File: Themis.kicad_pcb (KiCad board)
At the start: 2 copper layers, 100 x 50 mm, 568 parts, among them J1 SMA, J10 Conn_01x01, J11 Conn_01x01, J12 Conn_01x01, J13 Conn_01x01, J14 SMA, J15 SMA, J16 SMA, J17 SMA, J18 Conn_01x01, J2 SMA, J20 Conn_01x01, J3 SMA, J4 SMA, J5 Conn_01x05, J6 SMA, J7 SMA, J8 SMA, J9 SMA, T1 Tr 1/33, T2 Tr 33/1, U1 LMC6482

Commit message: preparing themis v2
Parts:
- removed C6: 10n, Capacitors_SMD:C_0805_HandSoldering
- removed J1, J14, J3, J6: SMA, SMA_PINS:SMA_EDGE_NRW
- removed J15, J16, J2, J4, J9: SMA, SMA_PINS:SMA_PINS
- removed L1: L_Small, Inductors_SMD:L_0805_HandSoldering
- removed the REF** at (186.0, 94.0)
- removed the REF** at (187.0, 98.0)
- removed the REF** at (120.0, 90.0)
- removed the REF** at (119.0, 90.0)
- removed the REF** at (118.0, 90.0)
- removed the REF** at (117.0, 90.0)
- removed the REF** at (116.0, 90.0)
- removed the REF** at (115.0, 90.0)
- removed the REF** at (114.0, 90.0)
- removed the REF** at (113.0, 90.0)
- removed the REF** at (112.0, 90.0)
- removed the REF** at (111.0, 90.0)
- removed the REF** at (186.0, 99.0)
- removed the REF** at (110.0, 90.0)
- removed the REF** at (109.0, 90.0)
- removed the REF** at (108.0, 90.0)
- removed the REF** at (107.0, 90.0)
- removed the REF** at (106.0, 90.0)
- removed the REF** at (105.0, 90.0)
- removed the REF** at (104.0, 90.0)
- removed the REF** at (103.0, 90.0)
- removed the REF** at (102.0, 90.0)
- removed the REF** at (101.0, 90.0)
- removed the REF** at (187.0, 99.0)
- removed the REF** at (100.0, 90.0)
- removed the REF** at (99.0, 90.0)
- removed the REF** at (127.0, 89.0)
- removed the REF** at (126.0, 89.0)
- removed the REF** at (125.0, 89.0)
- removed the REF** at (124.0, 89.0)
- removed the REF** at (123.0, 89.0)
- removed the REF** at (122.0, 89.0)
- removed the REF** at (121.0, 89.0)
- removed the REF** at (120.0, 89.0)
- removed the REF** at (186.0, 100.0)
- removed the REF** at (119.0, 89.0)
- removed the REF** at (118.0, 89.0)
- removed the REF** at (117.0, 89.0)
- removed the REF** at (116.0, 89.0)
- removed the REF** at (115.0, 89.0)
- removed the REF** at (114.0, 89.0)
- removed the REF** at (113.0, 89.0)
- removed the REF** at (112.0, 89.0)
- removed the REF** at (111.0, 89.0)
- removed the REF** at (110.0, 89.0)
- removed the REF** at (187.0, 100.0)
- removed the REF** at (109.0, 89.0)
- removed the REF** at (108.0, 89.0)
- removed the REF** at (107.0, 89.0)
- removed the REF** at (106.0, 89.0)
- removed the REF** at (105.0, 89.0)
- removed the REF** at (104.0, 89.0)
- removed the REF** at (103.0, 89.0)
- removed the REF** at (102.0, 89.0)
- removed the REF** at (101.0, 89.0)
- removed the REF** at (100.0, 89.0)
- removed the REF** at (188.0, 94.0)
- removed the REF** at (99.0, 89.0)
- removed the REF** at (127.0, 88.0)
- removed the REF** at (126.0, 88.0)
- removed the REF** at (125.0, 88.0)
- removed the REF** at (124.0, 88.0)
- removed the REF** at (123.0, 88.0)
- removed the REF** at (122.0, 88.0)
- removed the REF** at (121.0, 88.0)
- removed the REF** at (120.0, 88.0)
- removed the REF** at (119.0, 88.0)
- removed the REF** at (188.0, 95.0)
- removed the REF** at (118.0, 88.0)
- removed the REF** at (117.0, 88.0)
- removed the REF** at (116.0, 88.0)
- removed the REF** at (115.0, 88.0)
- removed the REF** at (114.0, 88.0)
- removed the REF** at (113.0, 88.0)
- removed the REF** at (112.0, 88.0)
- removed the REF** at (111.0, 88.0)
- removed the REF** at (110.0, 88.0)
- removed the REF** at (109.0, 88.0)
- removed the REF** at (188.0, 96.0)
- removed the REF** at (108.0, 88.0)
- removed the REF** at (107.0, 88.0)
- removed the REF** at (106.0, 88.0)
- removed the REF** at (105.0, 88.0)
- removed the REF** at (104.0, 88.0)
- removed the REF** at (103.0, 88.0)
- removed the REF** at (102.0, 88.0)
- removed the REF** at (101.0, 88.0)
- removed the REF** at (100.0, 88.0)
- removed the REF** at (99.0, 88.0)
- removed the REF** at (188.0, 97.0)
- removed the REF** at (127.0, 87.0)
- removed the REF** at (126.0, 87.0)
- removed the REF** at (125.0, 87.0)
- removed the REF** at (124.0, 87.0)
- removed the REF** at (123.0, 87.0)
- removed the REF** at (122.0, 87.0)
- removed the REF** at (121.0, 87.0)
- removed the REF** at (120.0, 87.0)
- removed the REF** at (119.0, 87.0)
- removed the REF** at (118.0, 87.0)
- removed the REF** at (188.0, 98.0)
- removed the REF** at (117.0, 87.0)
- removed the REF** at (116.0, 87.0)
- removed the REF** at (115.0, 87.0)
- removed the REF** at (114.0, 87.0)
- removed the REF** at (113.0, 87.0)
- removed the REF** at (112.0, 87.0)
- removed the REF** at (111.0, 87.0)
- removed the REF** at (110.0, 87.0)
- removed the REF** at (109.0, 87.0)
- removed the REF** at (108.0, 87.0)
- removed the REF** at (187.0, 94.0)
- removed the REF** at (188.0, 99.0)
- removed the REF** at (107.0, 87.0)
- removed the REF** at (106.0, 87.0)
- removed the REF** at (105.0, 87.0)
- removed the REF** at (104.0, 87.0)
- removed the REF** at (103.0, 87.0)
- removed the REF** at (102.0, 87.0)
- removed the REF** at (101.0, 87.0)
- removed the REF** at (100.0, 87.0)
- removed the REF** at (99.0, 87.0)
- removed the REF** at (91.0, 101.0)
- removed the REF** at (188.0, 100.0)
- removed the REF** at (91.0, 100.0)
- removed the REF** at (91.0, 99.0)
- removed the REF** at (91.0, 98.0)
- removed the REF** at (91.0, 97.0)
- removed the REF** at (91.0, 96.0)
- removed the REF** at (91.0, 95.0)
- removed the REF** at (91.0, 94.0)
- removed the REF** at (91.0, 93.0)
- removed the REF** at (91.0, 92.0)
- removed the REF** at (91.0, 91.0)
- removed the REF** at (93.0, 94.0)
- removed the REF** at (91.0, 90.0)
- removed the REF** at (91.0, 89.0)
- removed the REF** at (91.0, 88.0)
- removed the REF** at (91.0, 87.0)
- removed the REF** at (189.0, 101.0)
- removed the REF** at (189.0, 100.0)
- removed the REF** at (189.0, 99.0)
- removed the REF** at (189.0, 98.0)
- removed the REF** at (189.0, 97.0)
- removed the REF** at (189.0, 96.0)
- removed the REF** at (94.0, 94.0)
- removed the REF** at (189.0, 95.0)
- removed the REF** at (189.0, 94.0)
- removed the REF** at (189.0, 93.0)
- removed the REF** at (189.0, 92.0)
- removed the REF** at (189.0, 91.0)
- removed the REF** at (189.0, 90.0)
- removed the REF** at (189.0, 89.0)
- removed the REF** at (189.0, 88.0)
- removed the REF** at (189.0, 87.0)
- removed the REF** at (189.0, 133.0)
- removed the REF** at (95.0, 94.0)
- removed the REF** at (189.0, 132.0)
- removed the REF** at (189.0, 131.0)
- removed the REF** at (189.0, 130.0)
- removed the REF** at (189.0, 129.0)
- removed the REF** at (189.0, 128.0)
- removed the REF** at (189.0, 127.0)
- removed the REF** at (189.0, 126.0)
- removed the REF** at (189.0, 125.0)
- removed the REF** at (189.0, 124.0)
- removed the REF** at (189.0, 123.0)
- removed the REF** at (93.0, 95.0)
- removed the REF** at (189.0, 122.0)
- removed the REF** at (189.0, 121.0)
- removed the REF** at (189.0, 120.0)
- removed the REF** at (189.0, 119.0)
- removed the REF** at (189.0, 118.0)
- removed the REF** at (189.0, 117.0)
- removed the REF** at (189.0, 116.0)
- removed the REF** at (189.0, 115.0)
- removed the REF** at (189.0, 114.0)
- removed the REF** at (189.0, 113.0)
- removed the REF** at (94.0, 95.0)
- removed the REF** at (189.0, 112.0)
- removed the REF** at (189.0, 111.0)
- removed the REF** at (189.0, 110.0)
- removed the REF** at (188.5, 134.0)
- removed the REF** at (187.5, 134.0)
- removed the REF** at (186.5, 134.0)
- removed the REF** at (185.5, 134.0)
- removed the REF** at (184.5, 134.0)
- removed the REF** at (183.5, 134.0)
- removed the REF** at (182.5, 134.0)
- removed the REF** at (95.0, 95.0)
- removed the REF** at (181.5, 134.0)
- removed the REF** at (180.5, 134.0)
- removed the REF** at (179.5, 134.0)
- removed the REF** at (178.5, 134.0)
- removed the REF** at (177.5, 134.0)
- removed the REF** at (176.5, 134.0)
- removed the REF** at (168.5, 134.0)
- removed the REF** at (167.5, 134.0)
- removed the REF** at (166.5, 134.0)
- removed the REF** at (165.5, 134.0)
- removed the REF** at (93.0, 96.0)
- removed the REF** at (164.5, 134.0)
- removed the REF** at (163.5, 134.0)
- removed the REF** at (162.5, 134.0)
- removed the REF** at (161.5, 134.0)
- removed the REF** at (160.5, 134.0)
- removed the REF** at (159.5, 134.0)
- removed the REF** at (158.5, 134.0)
- removed the REF** at (157.5, 134.0)
- removed the REF** at (156.5, 134.0)
- removed the REF** at (155.5, 134.0)
- removed the REF** at (94.0, 96.0)
- removed the REF** at (154.5, 134.0)
- removed the REF** at (153.5, 134.0)
- removed the REF** at (152.5, 134.0)
- removed the REF** at (151.5, 134.0)
- removed the REF** at (150.5, 134.0)
- removed the REF** at (149.5, 134.0)
- removed the REF** at (148.5, 134.0)
- removed the REF** at (147.5, 134.0)
- removed the REF** at (146.5, 134.0)
- removed the REF** at (145.5, 134.0)
- removed the REF** at (186.0, 95.0)
- removed the REF** at (95.0, 96.0)
- removed the REF** at (144.5, 134.0)
- removed the REF** at (143.5, 134.0)
- removed the REF** at (142.5, 134.0)
- removed the REF** at (141.5, 134.0)
- removed the REF** at (104.5, 134.0)
- removed the REF** at (103.5, 134.0)
- removed the REF** at (102.5, 134.0)
- removed the REF** at (101.5, 134.0)
- removed the REF** at (100.5, 134.0)
- removed the REF** at (99.5, 134.0)
- removed the REF** at (93.0, 97.0)
- removed the REF** at (98.5, 134.0)
- removed the REF** at (97.5, 134.0)
- removed the REF** at (96.5, 134.0)
- removed the REF** at (95.5, 134.0)
- removed the REF** at (94.5, 134.0)
- removed the REF** at (93.5, 134.0)
- removed the REF** at (92.5, 134.0)
- removed the REF** at (91.5, 134.0)
- removed the REF** at (91.5, 133.0)
- removed the REF** at (91.5, 132.0)
- removed the REF** at (94.0, 97.0)
- removed the REF** at (91.5, 131.0)
- removed the REF** at (91.5, 130.0)
- removed the REF** at (91.5, 129.0)
- removed the REF** at (91.5, 128.0)
- removed the REF** at (91.5, 127.0)
- removed the REF** at (91.5, 126.0)
- removed the REF** at (91.5, 125.0)
- removed the REF** at (91.5, 124.0)
- removed the REF** at (91.5, 123.0)
- removed the REF** at (91.5, 122.0)
- removed the REF** at (95.0, 97.0)
- removed the REF** at (91.5, 121.0)
- removed the REF** at (91.5, 120.0)
- removed the REF** at (91.5, 119.0)
- removed the REF** at (91.5, 118.0)
- removed the REF** at (91.5, 117.0)
- removed the REF** at (91.5, 116.0)
- removed the REF** at (91.5, 115.0)
- removed the REF** at (91.5, 114.0)
- removed the REF** at (91.5, 113.0)
- removed the REF** at (91.5, 112.0)
- removed the REF** at (93.0, 98.0)
- removed the REF** at (91.5, 111.0)
- removed the REF** at (91.5, 110.0)
- removed the REF** at (91.5, 109.0)
- removed the REF** at (189.0, 86.0)
- removed the REF** at (188.0, 86.0)
- removed the REF** at (187.0, 86.0)
- removed the REF** at (186.0, 86.0)
- removed the REF** at (185.0, 86.0)
- removed the REF** at (184.0, 86.0)
- removed the REF** at (183.0, 86.0)
- removed the REF** at (94.0, 98.0)
- removed the REF** at (182.0, 86.0)
- removed the REF** at (181.0, 86.0)
- removed the REF** at (180.0, 86.0)
- removed the REF** at (179.0, 86.0)
- removed the REF** at (178.0, 86.0)
- removed the REF** at (177.0, 86.0)
- removed the REF** at (176.0, 86.0)
- removed the REF** at (175.0, 86.0)
- removed the REF** at (174.0, 86.0)
- removed the REF** at (173.0, 86.0)
- removed the REF** at (95.0, 98.0)
- removed the REF** at (172.0, 86.0)
- removed the REF** at (171.0, 86.0)
- removed the REF** at (170.0, 86.0)
- removed the REF** at (169.0, 86.0)
- removed the REF** at (168.0, 86.0)
- removed the REF** at (167.0, 86.0)
- removed the REF** at (166.0, 86.0)
- removed the REF** at (165.0, 86.0)
- removed the REF** at (164.0, 86.0)
- removed the REF** at (163.0, 86.0)
- removed the REF** at (93.0, 99.0)
- removed the REF** at (162.0, 86.0)
- removed the REF** at (161.0, 86.0)
- removed the REF** at (160.0, 86.0)
- removed the REF** at (159.0, 86.0)
- removed the REF** at (158.0, 86.0)
- removed the REF** at (157.0, 86.0)
- removed the REF** at (156.0, 86.0)
- removed the REF** at (155.0, 86.0)
- removed the REF** at (154.0, 86.0)
- removed the REF** at (153.0, 86.0)
- removed the REF** at (94.0, 99.0)
- removed the REF** at (152.0, 86.0)
- removed the REF** at (151.0, 86.0)
- removed the REF** at (150.0, 86.0)
- removed the REF** at (149.0, 86.0)
- removed the REF** at (148.0, 86.0)
- removed the REF** at (147.0, 86.0)
- removed the REF** at (146.0, 86.0)
- removed the REF** at (145.0, 86.0)
- removed the REF** at (144.0, 86.0)
- removed the REF** at (143.0, 86.0)
- removed the REF** at (95.0, 99.0)
- removed the REF** at (142.0, 86.0)
- removed the REF** at (141.0, 86.0)
- removed the REF** at (140.0, 86.0)
- removed the REF** at (139.0, 86.0)
- removed the REF** at (138.0, 86.0)
- removed the REF** at (137.0, 86.0)
- removed the REF** at (136.0, 86.0)
- removed the REF** at (135.0, 86.0)
- removed the REF** at (134.0, 86.0)
- removed the REF** at (133.0, 86.0)
- removed the REF** at (187.0, 95.0)
- removed the REF** at (92.0, 94.0)
- removed the REF** at (132.0, 86.0)
- removed the REF** at (131.0, 86.0)
- removed the REF** at (130.0, 86.0)
- removed the REF** at (129.0, 86.0)
- removed the REF** at (128.0, 86.0)
- removed the REF** at (127.0, 86.0)
- removed the REF** at (126.0, 86.0)
- removed the REF** at (125.0, 86.0)
- removed the REF** at (124.0, 86.0)
- removed the REF** at (123.0, 86.0)
- removed the REF** at (92.0, 95.0)
- removed the REF** at (122.0, 86.0)
- removed the REF** at (121.0, 86.0)
- removed the REF** at (120.0, 86.0)
- removed the REF** at (119.0, 86.0)
- removed the REF** at (118.0, 86.0)
- removed the REF** at (117.0, 86.0)
- removed the REF** at (116.0, 86.0)
- removed the REF** at (115.0, 86.0)
- removed the REF** at (114.0, 86.0)
- removed the REF** at (113.0, 86.0)
- removed the REF** at (92.0, 96.0)
- removed the REF** at (112.0, 86.0)
- removed the REF** at (111.0, 86.0)
- removed the REF** at (110.0, 86.0)
- removed the REF** at (109.0, 86.0)
- removed the REF** at (108.0, 86.0)
- removed the REF** at (107.0, 86.0)
- removed the REF** at (106.0, 86.0)
- removed the REF** at (105.0, 86.0)
- removed the REF** at (104.0, 86.0)
- removed the REF** at (103.0, 86.0)
- removed the REF** at (92.0, 97.0)
- removed the REF** at (102.0, 86.0)
- removed the REF** at (101.0, 86.0)
- removed the REF** at (100.0, 86.0)
- removed the REF** at (99.0, 86.0)
- removed the REF** at (98.0, 86.0)
- removed the REF** at (97.0, 86.0)
- removed the REF** at (96.0, 86.0)
- removed the REF** at (95.0, 86.0)
- removed the REF** at (94.0, 86.0)
- removed the REF** at (93.0, 86.0)
- removed the REF** at (92.0, 98.0)
- removed the REF** at (92.0, 86.0)
- removed the REF** at (94.5, 126.0)
- removed the REF** at (93.5, 126.0)
- removed the REF** at (92.5, 126.0)
- removed the REF** at (94.5, 125.0)
- removed the REF** at (93.5, 125.0)
- removed the REF** at (92.5, 125.0)
- removed the REF** at (94.5, 124.0)
- removed the REF** at (93.5, 124.0)
- removed the REF** at (92.5, 124.0)
- removed the REF** at (92.0, 99.0)
- removed the REF** at (94.5, 123.0)
- removed the REF** at (93.5, 123.0)
- removed the REF** at (92.5, 123.0)
- removed the REF** at (94.5, 122.0)
- removed the REF** at (93.5, 122.0)
- removed the REF** at (92.5, 122.0)
- removed the REF** at (94.5, 121.0)
- removed the REF** at (93.5, 121.0)
- removed the REF** at (92.5, 121.0)
- removed the REF** at (94.5, 120.0)
- removed the REF** at (188.0, 128.0)
- removed the REF** at (93.5, 120.0)
- removed the REF** at (92.5, 120.0)
- removed the REF** at (94.5, 119.0)
- removed the REF** at (93.5, 119.0)
- removed the REF** at (92.5, 119.0)
- removed the REF** at (94.5, 118.0)
- removed the REF** at (93.5, 118.0)
- removed the REF** at (92.5, 118.0)
- removed the REF** at (94.5, 117.0)
- removed the REF** at (93.5, 117.0)
- removed the REF** at (188.0, 127.0)
- removed the REF** at (92.5, 117.0)
- removed the REF** at (94.5, 116.0)
- removed the REF** at (93.5, 116.0)
- removed the REF** at (92.5, 116.0)
- removed the REF** at (94.5, 115.0)
- removed the REF** at (93.5, 115.0)
- removed the REF** at (92.5, 115.0)
- removed the REF** at (94.5, 114.0)
- removed the REF** at (93.5, 114.0)
- removed the REF** at (92.5, 114.0)
- removed the REF** at (188.0, 126.0)
- removed the REF** at (94.5, 113.0)
- removed the REF** at (93.5, 113.0)
- removed the REF** at (92.5, 113.0)
- removed the REF** at (94.5, 112.0)
- removed the REF** at (93.5, 112.0)
- removed the REF** at (92.5, 112.0)
- removed the REF** at (94.5, 111.0)
- removed the REF** at (93.5, 111.0)
- removed the REF** at (187.0, 126.0)
- removed the REF** at (186.0, 126.0)
- removed the REF** at (188.0, 125.0)
- removed the REF** at (187.0, 125.0)
- removed the REF** at (186.0, 125.0)
- removed the REF** at (187.0, 124.0)
- removed the REF** at (186.0, 124.0)
- removed the REF** at (187.0, 123.0)
- removed the REF** at (186.0, 123.0)
- removed the REF** at (187.0, 122.0)
- removed the REF** at (186.0, 122.0)
- removed the REF** at (187.0, 121.0)
- removed the REF** at (186.0, 121.0)
- removed the REF** at (186.0, 96.0)
- removed the REF** at (188.0, 124.0)
- removed the REF** at (187.0, 120.0)
- removed the REF** at (186.0, 120.0)
- removed the REF** at (187.0, 119.0)
- removed the REF** at (186.0, 119.0)
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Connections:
- J5 pad 5: TX_RX_RLY -> (no net)
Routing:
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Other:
- board text added: "Themis Θέμις V2.0"
- board text removed: "HPF out"
- board text removed: "PS_IN"
- board text removed: "RX1_Line"
- board text removed: "Themis Θέμις"

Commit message: Themis V2
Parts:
- removed REF**: via, via:via
- C2, C3, C4, C5, D1, D2, D3, D4, R10, R11, R12, R13, R4, R5, R6, R7, R8, R9: moved to B.Cu
- J17, J8: footprint SMA_PINS:SMA_EDGE_NRW -> SMA_PINS:SMA_PINS
- U1: footprint Housings_SOIC:SOIC-8_3.9x4.9mm_Pitch1.27mm -> Package_SO:SOIC-8_3.9x4.9mm_P1.27mm; moved to B.Cu
- moved R6 19.7 mm to (149.5, 127.0), turned to 180 degrees
- moved J5 17.0 mm to (143.0, 130.5)
- moved C3 12.3 mm to (160.5, 123.0), turned to 270 degrees
- moved R11 12.0 mm to (158.5, 118.0), turned to 90 degrees
- moved D2 11.8 mm to (155.0, 126.0), turned to 270 degrees
- moved C2 10.1 mm to (155.2, 131.5), turned to 90 degrees
- moved T1 10.0 mm to (170.0, 105.0)
- moved R7 9.71 mm to (163.0, 123.0), turned to 270 degrees
- moved R5 9.49 mm to (159.5, 131.5), turned to 270 degrees
- moved U1 8.85 mm to (150.0, 121.5), turned to 90 degrees
- moved R12 8.50 mm to (142.0, 122.5), turned to 90 degrees
- moved R9 8.06 mm to (130.5, 118.5), turned to 180 degrees
- moved D1 8.00 mm to (161.5, 118.0), turned to 180 degrees
- moved R10 7.50 mm to (134.0, 115.0)
- moved R8 7.50 mm to (138.5, 114.5)
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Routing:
- net GND: track 375.5 -> 308.9 mm, vias 312 -> 258
- net (no net): track 27.1 -> 3.05 mm, vias 21 -> 0
- net Net-(J8-Pad1): track 23.5 -> 8.51 mm
- net Net-(C2-Pad2): track 10.1 -> 23.7 mm
- net Net-(C3-Pad1): track 9.81 -> 19.8 mm
- net Net-(D1-Pad2): track 37.9 -> 29.7 mm
- net +12V: track 18.8 -> 26.3 mm
- net Net-(C1-Pad2): track 74.0 -> 81.2 mm
- net Net-(D4-Pad2): track 7.96 -> 14.8 mm
- net Net-(D2-Pad2): track 8.36 -> 11.4 mm
- net Net-(C4-Pad1): track 16.8 -> 13.8 mm
- net Net-(D3-Pad2): track 9.31 -> 6.82 mm
- net Net-(C5-Pad2): track 12.9 -> 11.3 mm
- net Net-(D4-Pad1): track 10.1 -> 11.5 mm
- net Net-(D2-Pad1): track 11.8 -> 10.5 mm
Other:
- board text added: "In"
- board text added: "LPF_ Out"
- board text added: "Out"
- board text added: "PS_ Feedback"
- board text added: "TX_ Coax_ Out"
- board text removed: "LPF_Out"
- board text removed: "PS_Feedback"
- board text removed: "TX_Coax_Out"

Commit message: new heavy duty stitching
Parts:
- added REF**: via, via:via, F.Cu at (181.0, 91.0)
- added REF**: via, via:via, F.Cu at (163.0, 91.0)
- added REF**: via, via:via, F.Cu at (102.0, 100.0)
- added REF**: via, via:via, F.Cu at (100.0, 100.0)
- added REF**: via, via:via, F.Cu at (98.0, 100.0)
- added REF**: via, via:via, F.Cu at (96.0, 100.0)
- added REF**: via, via:via, F.Cu at (94.0, 100.0)
- added REF**: via, via:via, F.Cu at (92.0, 100.0)
- added REF**: via, via:via, F.Cu at (132.0, 98.0)
- added REF**: via, via:via, F.Cu at (130.0, 98.0)
- added REF**: via, via:via, F.Cu at (128.0, 98.0)
- added REF**: via, via:via, F.Cu at (126.0, 98.0)
- added REF**: via, via:via, F.Cu at (161.0, 91.0)
- added REF**: via, via:via, F.Cu at (124.0, 98.0)
- added REF**: via, via:via, F.Cu at (122.0, 98.0)
- added REF**: via, via:via, F.Cu at (120.0, 98.0)
- added REF**: via, via:via, F.Cu at (118.0, 98.0)
- added REF**: via, via:via, F.Cu at (116.0, 98.0)
- added REF**: via, via:via, F.Cu at (108.0, 98.0)
- added REF**: via, via:via, F.Cu at (106.0, 98.0)
- added REF**: via, via:via, F.Cu at (104.0, 98.0)
- added REF**: via, via:via, F.Cu at (102.0, 98.0)
- added REF**: via, via:via, F.Cu at (100.0, 98.0)
- added REF**: via, via:via, F.Cu at (159.0, 91.0)
- added REF**: via, via:via, F.Cu at (98.0, 98.0)
- added REF**: via, via:via, F.Cu at (96.0, 98.0)
- added REF**: via, via:via, F.Cu at (94.0, 98.0)
- added REF**: via, via:via, F.Cu at (92.0, 98.0)
- added REF**: via, via:via, F.Cu at (132.0, 96.0)
- added REF**: via, via:via, F.Cu at (130.0, 96.0)
- added REF**: via, via:via, F.Cu at (128.0, 96.0)
- added REF**: via, via:via, F.Cu at (126.0, 96.0)
- added REF**: via, via:via, F.Cu at (124.0, 96.0)
- added REF**: via, via:via, F.Cu at (122.0, 96.0)
- added REF**: via, via:via, F.Cu at (157.0, 91.0)
- added REF**: via, via:via, F.Cu at (120.0, 96.0)
- added REF**: via, via:via, F.Cu at (118.0, 96.0)
- added REF**: via, via:via, F.Cu at (116.0, 96.0)
- added REF**: via, via:via, F.Cu at (114.0, 96.0)
- added REF**: via, via:via, F.Cu at (112.0, 96.0)
- added REF**: via, via:via, F.Cu at (110.0, 96.0)
- added REF**: via, via:via, F.Cu at (108.0, 96.0)
- added REF**: via, via:via, F.Cu at (106.0, 96.0)
- added REF**: via, via:via, F.Cu at (104.0, 96.0)
- added REF**: via, via:via, F.Cu at (102.0, 96.0)
- added REF**: via, via:via, F.Cu at (155.0, 91.0)
- added REF**: via, via:via, F.Cu at (100.0, 96.0)
- added REF**: via, via:via, F.Cu at (98.0, 96.0)
- added REF**: via, via:via, F.Cu at (96.0, 96.0)
- added REF**: via, via:via, F.Cu at (94.0, 96.0)
- added REF**: via, via:via, F.Cu at (92.0, 96.0)
- added REF**: via, via:via, F.Cu at (132.0, 94.0)
- added REF**: via, via:via, F.Cu at (130.0, 94.0)
- added REF**: via, via:via, F.Cu at (128.0, 94.0)
- added REF**: via, via:via, F.Cu at (126.0, 94.0)
- added REF**: via, via:via, F.Cu at (124.0, 94.0)
- added REF**: via, via:via, F.Cu at (153.0, 91.0)
- added REF**: via, via:via, F.Cu at (122.0, 94.0)
- added REF**: via, via:via, F.Cu at (120.0, 94.0)
- added REF**: via, via:via, F.Cu at (118.0, 94.0)
- added REF**: via, via:via, F.Cu at (116.0, 94.0)
- added REF**: via, via:via, F.Cu at (114.0, 94.0)
- added REF**: via, via:via, F.Cu at (112.0, 94.0)
- added REF**: via, via:via, F.Cu at (110.0, 94.0)
- added REF**: via, via:via, F.Cu at (108.0, 94.0)
- added REF**: via, via:via, F.Cu at (106.0, 94.0)
- added REF**: via, via:via, F.Cu at (104.0, 94.0)
- added REF**: via, via:via, F.Cu at (151.0, 91.0)
- added REF**: via, via:via, F.Cu at (102.0, 94.0)
- added REF**: via, via:via, F.Cu at (100.0, 94.0)
- added REF**: via, via:via, F.Cu at (98.0, 94.0)
- added REF**: via, via:via, F.Cu at (96.0, 94.0)
- added REF**: via, via:via, F.Cu at (94.0, 94.0)
- added REF**: via, via:via, F.Cu at (92.0, 94.0)
- added REF**: via, via:via, F.Cu at (132.0, 92.0)
- added REF**: via, via:via, F.Cu at (130.0, 92.0)
- added REF**: via, via:via, F.Cu at (128.0, 92.0)
- added REF**: via, via:via, F.Cu at (126.0, 92.0)
- added REF**: via, via:via, F.Cu at (149.0, 91.0)
- added REF**: via, via:via, F.Cu at (124.0, 92.0)
- added REF**: via, via:via, F.Cu at (122.0, 92.0)
- added REF**: via, via:via, F.Cu at (120.0, 92.0)
- added REF**: via, via:via, F.Cu at (118.0, 92.0)
- added REF**: via, via:via, F.Cu at (116.0, 92.0)
- added REF**: via, via:via, F.Cu at (114.0, 92.0)
- added REF**: via, via:via, F.Cu at (112.0, 92.0)
- added REF**: via, via:via, F.Cu at (110.0, 92.0)
- added REF**: via, via:via, F.Cu at (108.0, 92.0)
- added REF**: via, via:via, F.Cu at (106.0, 92.0)
- added REF**: via, via:via, F.Cu at (147.0, 91.0)
- added REF**: via, via:via, F.Cu at (104.0, 92.0)
- added REF**: via, via:via, F.Cu at (102.0, 92.0)
- added REF**: via, via:via, F.Cu at (100.0, 92.0)
- added REF**: via, via:via, F.Cu at (133.0, 126.0)
- added REF**: via, via:via, F.Cu at (131.0, 126.0)
- added REF**: via, via:via, F.Cu at (129.0, 126.0)
- added REF**: via, via:via, F.Cu at (127.0, 126.0)
- added REF**: via, via:via, F.Cu at (133.0, 124.0)
- added REF**: via, via:via, F.Cu at (131.0, 124.0)
- added REF**: via, via:via, F.Cu at (129.0, 124.0)
- added REF**: via, via:via, F.Cu at (147.0, 93.0)
- added REF**: via, via:via, F.Cu at (127.0, 124.0)
- added REF**: via, via:via, F.Cu at (151.0, 133.0)
- added REF**: via, via:via, F.Cu at (149.0, 133.0)
- added REF**: via, via:via, F.Cu at (147.0, 133.0)
- added REF**: via, via:via, F.Cu at (151.0, 131.0)
- added REF**: via, via:via, F.Cu at (149.0, 131.0)
- added REF**: via, via:via, F.Cu at (147.0, 131.0)
- added REF**: via, via:via, F.Cu at (181.0, 133.0)
- added REF**: via, via:via, F.Cu at (179.0, 133.0)
- added REF**: via, via:via, F.Cu at (177.0, 133.0)
- added REF**: via, via:via, F.Cu at (179.0, 91.0)
- added REF**: via, via:via, F.Cu at (149.0, 93.0)
- added REF**: via, via:via, F.Cu at (175.0, 133.0)
- added REF**: via, via:via, F.Cu at (173.0, 133.0)
- added REF**: via, via:via, F.Cu at (181.0, 131.0)
- added REF**: via, via:via, F.Cu at (179.0, 131.0)
- added REF**: via, via:via, F.Cu at (177.0, 131.0)
- added REF**: via, via:via, F.Cu at (175.0, 131.0)
- added REF**: via, via:via, F.Cu at (173.0, 131.0)
- added REF**: via, via:via, F.Cu at (124.0, 133.0)
- added REF**: via, via:via, F.Cu at (122.0, 133.0)
- added REF**: via, via:via, F.Cu at (120.0, 133.0)
- added REF**: via, via:via, F.Cu at (151.0, 93.0)
- added REF**: via, via:via, F.Cu at (118.0, 133.0)
- added REF**: via, via:via, F.Cu at (116.0, 133.0)
- added REF**: via, via:via, F.Cu at (114.0, 133.0)
- added REF**: via, via:via, F.Cu at (112.0, 133.0)
- added REF**: via, via:via, F.Cu at (110.0, 133.0)
- added REF**: via, via:via, F.Cu at (108.0, 133.0)
- added REF**: via, via:via, F.Cu at (106.0, 133.0)
- added REF**: via, via:via, F.Cu at (104.0, 133.0)
- added REF**: via, via:via, F.Cu at (102.0, 133.0)
- added REF**: via, via:via, F.Cu at (100.0, 133.0)
- added REF**: via, via:via, F.Cu at (153.0, 93.0)
- added REF**: via, via:via, F.Cu at (124.0, 131.0)
- added REF**: via, via:via, F.Cu at (122.0, 131.0)
- added REF**: via, via:via, F.Cu at (120.0, 131.0)
- added REF**: via, via:via, F.Cu at (118.0, 131.0)
- added REF**: via, via:via, F.Cu at (116.0, 131.0)
- added REF**: via, via:via, F.Cu at (114.0, 131.0)
- added REF**: via, via:via, F.Cu at (112.0, 131.0)
- added REF**: via, via:via, F.Cu at (110.0, 131.0)
- added REF**: via, via:via, F.Cu at (108.0, 131.0)
- added REF**: via, via:via, F.Cu at (106.0, 131.0)
- added REF**: via, via:via, F.Cu at (155.0, 93.0)
- added REF**: via, via:via, F.Cu at (104.0, 131.0)
- added REF**: via, via:via, F.Cu at (102.0, 131.0)
- added REF**: via, via:via, F.Cu at (100.0, 131.0)
- added REF**: via, via:via, F.Cu at (100.0, 124.0)
- added REF**: via, via:via, F.Cu at (102.0, 124.0)
- added REF**: via, via:via, F.Cu at (104.0, 124.0)
- added REF**: via, via:via, F.Cu at (106.0, 124.0)
- added REF**: via, via:via, F.Cu at (108.0, 124.0)
- added REF**: via, via:via, F.Cu at (110.0, 124.0)
- added REF**: via, via:via, F.Cu at (112.0, 124.0)
- added REF**: via, via:via, F.Cu at (157.0, 93.0)
- added REF**: via, via:via, F.Cu at (114.0, 124.0)
- added REF**: via, via:via, F.Cu at (116.0, 124.0)
- added REF**: via, via:via, F.Cu at (118.0, 124.0)
- added REF**: via, via:via, F.Cu at (120.0, 124.0)
- added REF**: via, via:via, F.Cu at (122.0, 124.0)
- added REF**: via, via:via, F.Cu at (124.0, 124.0)
- added REF**: via, via:via, F.Cu at (100.0, 126.0)
- added REF**: via, via:via, F.Cu at (102.0, 126.0)
- added REF**: via, via:via, F.Cu at (104.0, 126.0)
- added REF**: via, via:via, F.Cu at (106.0, 126.0)
- added REF**: via, via:via, F.Cu at (159.0, 93.0)
- added REF**: via, via:via, F.Cu at (108.0, 126.0)
- added REF**: via, via:via, F.Cu at (110.0, 126.0)
- added REF**: via, via:via, F.Cu at (112.0, 126.0)
- added REF**: via, via:via, F.Cu at (114.0, 126.0)
- added REF**: via, via:via, F.Cu at (116.0, 126.0)
- added REF**: via, via:via, F.Cu at (118.0, 126.0)
- added REF**: via, via:via, F.Cu at (120.0, 126.0)
- added REF**: via, via:via, F.Cu at (122.0, 126.0)
- added REF**: via, via:via, F.Cu at (124.0, 126.0)
- added REF**: via, via:via, F.Cu at (100.0, 128.0)
- added REF**: via, via:via, F.Cu at (161.0, 93.0)
- added REF**: via, via:via, F.Cu at (102.0, 128.0)
- added REF**: via, via:via, F.Cu at (104.0, 128.0)
- added REF**: via, via:via, F.Cu at (106.0, 128.0)
- added REF**: via, via:via, F.Cu at (108.0, 128.0)
- added REF**: via, via:via, F.Cu at (110.0, 128.0)
- added REF**: via, via:via, F.Cu at (112.0, 128.0)
- added REF**: via, via:via, F.Cu at (114.0, 128.0)
- added REF**: via, via:via, F.Cu at (116.0, 128.0)
- added REF**: via, via:via, F.Cu at (118.0, 128.0)
- added REF**: via, via:via, F.Cu at (120.0, 128.0)
- added REF**: via, via:via, F.Cu at (163.0, 93.0)
- added REF**: via, via:via, F.Cu at (122.0, 128.0)
- added REF**: via, via:via, F.Cu at (124.0, 128.0)
- added REF**: via, via:via, F.Cu at (124.0, 122.0)
- added REF**: via, via:via, F.Cu at (122.0, 122.0)
- added REF**: via, via:via, F.Cu at (120.0, 122.0)
- added REF**: via, via:via, F.Cu at (118.0, 122.0)
- added REF**: via, via:via, F.Cu at (116.0, 122.0)
- added REF**: via, via:via, F.Cu at (114.0, 122.0)
- added REF**: via, via:via, F.Cu at (112.0, 122.0)
- added REF**: via, via:via, F.Cu at (110.0, 122.0)
- added REF**: via, via:via, F.Cu at (165.0, 93.0)
- added REF**: via, via:via, F.Cu at (108.0, 122.0)
- added REF**: via, via:via, F.Cu at (106.0, 122.0)
- added REF**: via, via:via, F.Cu at (104.0, 122.0)
- added REF**: via, via:via, F.Cu at (102.0, 122.0)
- added REF**: via, via:via, F.Cu at (100.0, 122.0)
- added REF**: via, via:via, F.Cu at (98.0, 122.0)
- added REF**: via, via:via, F.Cu at (96.0, 122.0)
- added REF**: via, via:via, F.Cu at (94.0, 122.0)
- added REF**: via, via:via, F.Cu at (92.0, 122.0)
- added REF**: via, via:via, F.Cu at (124.0, 120.0)
- added REF**: via, via:via, F.Cu at (167.0, 93.0)
- added REF**: via, via:via, F.Cu at (122.0, 120.0)
- added REF**: via, via:via, F.Cu at (120.0, 120.0)
- added REF**: via, via:via, F.Cu at (118.0, 120.0)
- added REF**: via, via:via, F.Cu at (116.0, 120.0)
- added REF**: via, via:via, F.Cu at (114.0, 120.0)
- added REF**: via, via:via, F.Cu at (112.0, 120.0)
- added REF**: via, via:via, F.Cu at (110.0, 120.0)
- added REF**: via, via:via, F.Cu at (108.0, 120.0)
- added REF**: via, via:via, F.Cu at (106.0, 120.0)
- added REF**: via, via:via, F.Cu at (104.0, 120.0)
- added REF**: via, via:via, F.Cu at (177.0, 91.0)
- added REF**: via, via:via, F.Cu at (169.0, 93.0)
- added REF**: via, via:via, F.Cu at (102.0, 120.0)
- added REF**: via, via:via, F.Cu at (100.0, 120.0)
- added REF**: via, via:via, F.Cu at (98.0, 120.0)
- added REF**: via, via:via, F.Cu at (96.0, 120.0)
- added REF**: via, via:via, F.Cu at (94.0, 120.0)
- added REF**: via, via:via, F.Cu at (92.0, 120.0)
- added REF**: via, via:via, F.Cu at (124.0, 118.0)
- added REF**: via, via:via, F.Cu at (122.0, 118.0)
- added REF**: via, via:via, F.Cu at (120.0, 118.0)
- added REF**: via, via:via, F.Cu at (118.0, 118.0)
- added REF**: via, via:via, F.Cu at (171.0, 93.0)
- added REF**: via, via:via, F.Cu at (116.0, 118.0)
- added REF**: via, via:via, F.Cu at (114.0, 118.0)
- added REF**: via, via:via, F.Cu at (112.0, 118.0)
- added REF**: via, via:via, F.Cu at (110.0, 118.0)
- added REF**: via, via:via, F.Cu at (108.0, 118.0)
- added REF**: via, via:via, F.Cu at (106.0, 118.0)
- added REF**: via, via:via, F.Cu at (104.0, 118.0)
- added REF**: via, via:via, F.Cu at (102.0, 118.0)
- added REF**: via, via:via, F.Cu at (100.0, 118.0)
- added REF**: via, via:via, F.Cu at (98.0, 118.0)
- added REF**: via, via:via, F.Cu at (173.0, 93.0)
- added REF**: via, via:via, F.Cu at (96.0, 118.0)
- added REF**: via, via:via, F.Cu at (94.0, 118.0)
- added REF**: via, via:via, F.Cu at (92.0, 118.0)
- added REF**: via, via:via, F.Cu at (124.0, 116.0)
- added REF**: via, via:via, F.Cu at (122.0, 116.0)
- added REF**: via, via:via, F.Cu at (120.0, 116.0)
- added REF**: via, via:via, F.Cu at (118.0, 116.0)
- added REF**: via, via:via, F.Cu at (116.0, 116.0)
- added REF**: via, via:via, F.Cu at (114.0, 116.0)
- added REF**: via, via:via, F.Cu at (112.0, 116.0)
- added REF**: via, via:via, F.Cu at (175.0, 93.0)
- added REF**: via, via:via, F.Cu at (110.0, 116.0)
- added REF**: via, via:via, F.Cu at (108.0, 116.0)
- added REF**: via, via:via, F.Cu at (106.0, 116.0)
- added REF**: via, via:via, F.Cu at (104.0, 116.0)
- added REF**: via, via:via, F.Cu at (102.0, 116.0)
- added REF**: via, via:via, F.Cu at (100.0, 116.0)
- added REF**: via, via:via, F.Cu at (98.0, 116.0)
- added REF**: via, via:via, F.Cu at (96.0, 116.0)
- added REF**: via, via:via, F.Cu at (94.0, 116.0)
- added REF**: via, via:via, F.Cu at (92.0, 116.0)
- added REF**: via, via:via, F.Cu at (177.0, 93.0)
- added REF**: via, via:via, F.Cu at (124.0, 114.0)
- added REF**: via, via:via, F.Cu at (122.0, 114.0)
- added REF**: via, via:via, F.Cu at (120.0, 114.0)
- added REF**: via, via:via, F.Cu at (118.0, 114.0)
- added REF**: via, via:via, F.Cu at (116.0, 114.0)
- added REF**: via, via:via, F.Cu at (114.0, 114.0)
- added REF**: via, via:via, F.Cu at (112.0, 114.0)
- added REF**: via, via:via, F.Cu at (110.0, 114.0)
- added REF**: via, via:via, F.Cu at (108.0, 114.0)
- added REF**: via, via:via, F.Cu at (106.0, 114.0)
- added REF**: via, via:via, F.Cu at (179.0, 93.0)
- added REF**: via, via:via, F.Cu at (104.0, 114.0)
- added REF**: via, via:via, F.Cu at (102.0, 114.0)
- added REF**: via, via:via, F.Cu at (100.0, 114.0)
- added REF**: via, via:via, F.Cu at (98.0, 114.0)
- added REF**: via, via:via, F.Cu at (96.0, 114.0)
- added REF**: via, via:via, F.Cu at (94.0, 114.0)
- added REF**: via, via:via, F.Cu at (92.0, 114.0)
- added REF**: via, via:via, F.Cu at (124.0, 112.0)
- added REF**: via, via:via, F.Cu at (122.0, 112.0)
- added REF**: via, via:via, F.Cu at (120.0, 112.0)
- added REF**: via, via:via, F.Cu at (181.0, 93.0)
- added REF**: via, via:via, F.Cu at (118.0, 112.0)
- added REF**: via, via:via, F.Cu at (116.0, 112.0)
- added REF**: via, via:via, F.Cu at (114.0, 112.0)
- added REF**: via, via:via, F.Cu at (112.0, 112.0)
- added REF**: via, via:via, F.Cu at (110.0, 112.0)
- added REF**: via, via:via, F.Cu at (108.0, 112.0)
- added REF**: via, via:via, F.Cu at (106.0, 112.0)
- added REF**: via, via:via, F.Cu at (104.0, 112.0)
- added REF**: via, via:via, F.Cu at (102.0, 112.0)
- added REF**: via, via:via, F.Cu at (100.0, 112.0)
- added REF**: via, via:via, F.Cu at (147.0, 95.0)
- added REF**: via, via:via, F.Cu at (98.0, 112.0)
- added REF**: via, via:via, F.Cu at (96.0, 112.0)
- added REF**: via, via:via, F.Cu at (94.0, 112.0)
- added REF**: via, via:via, F.Cu at (92.0, 112.0)
- added REF**: via, via:via, F.Cu at (188.0, 126.0)
- added REF**: via, via:via, F.Cu at (186.0, 126.0)
- added REF**: via, via:via, F.Cu at (188.0, 100.0)
- added REF**: via, via:via, F.Cu at (186.0, 100.0)
- added REF**: via, via:via, F.Cu at (188.0, 124.0)
- added REF**: via, via:via, F.Cu at (186.0, 124.0)
- added REF**: via, via:via, F.Cu at (149.0, 95.0)
- added REF**: via, via:via, F.Cu at (188.0, 98.0)
- added REF**: via, via:via, F.Cu at (186.0, 98.0)
- added REF**: via, via:via, F.Cu at (188.0, 122.0)
- added REF**: via, via:via, F.Cu at (186.0, 122.0)
- added REF**: via, via:via, F.Cu at (188.0, 96.0)
- added REF**: via, via:via, F.Cu at (186.0, 96.0)
- added REF**: via, via:via, F.Cu at (188.0, 120.0)
- added REF**: via, via:via, F.Cu at (186.0, 120.0)
- added REF**: via, via:via, F.Cu at (188.0, 118.0)
- added REF**: via, via:via, F.Cu at (186.0, 118.0)
- added REF**: via, via:via, F.Cu at (151.0, 95.0)
- added REF**: via, via:via, F.Cu at (188.0, 116.0)
- added REF**: via, via:via, F.Cu at (186.0, 116.0)
- added REF**: via, via:via, F.Cu at (188.0, 114.0)
- added REF**: via, via:via, F.Cu at (186.0, 114.0)
- added REF**: via, via:via, F.Cu at (188.0, 112.0)
- added REF**: via, via:via, F.Cu at (186.0, 112.0)
- added REF**: via, via:via, F.Cu at (181.0, 89.0)
- added REF**: via, via:via, F.Cu at (179.0, 89.0)
- added REF**: via, via:via, F.Cu at (177.0, 89.0)
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
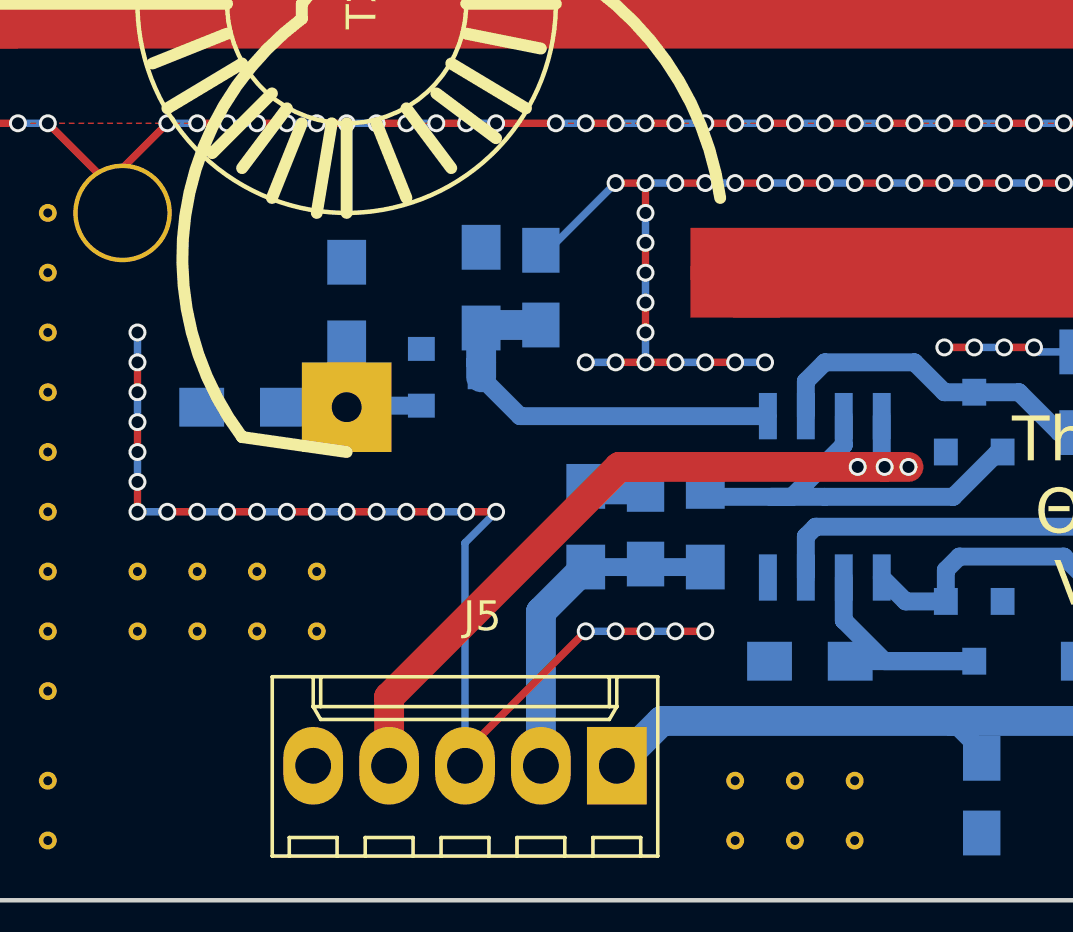
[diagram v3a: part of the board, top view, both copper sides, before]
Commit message: decoupling cap added in the op-amp power rail
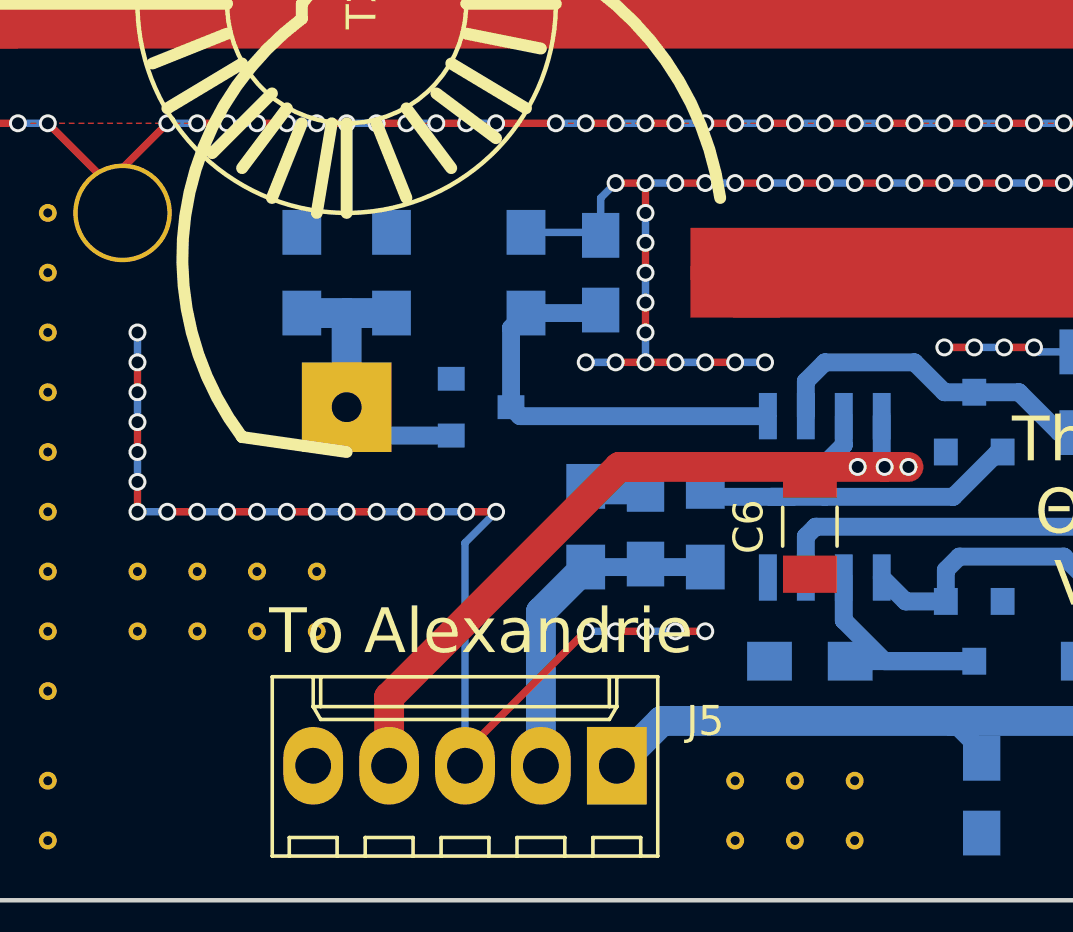
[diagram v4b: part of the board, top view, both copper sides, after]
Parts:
- added C6: 10n, Capacitor_SMD:C_1206_3216Metric_Pad1.24x1.80mm_HandSolder, F.Cu at (149.5, 122.5)
- moved R9 4.92 mm to (132.5, 114.0), turned to 90 degrees
- moved C4 2.06 mm to (142.5, 114.0)
- moved R10 1.80 mm to (135.5, 114.0)
- moved R8 1.58 mm to (140.0, 114.0)
- moved D3 1.41 mm to (138.5, 118.5)
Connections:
- J5 pad 5: (no net) -> Net-(J5-Pad5)
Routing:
- net Net-(D3-Pad2): track 6.82 -> 10.1 mm
- net +12V: track 26.3 -> 28.1 mm
- net GND: track 308.9 -> 309.9 mm
- net Net-(C4-Pad1): track 13.8 -> 14.6 mm
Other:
- board text added: "To Alexandrie"
